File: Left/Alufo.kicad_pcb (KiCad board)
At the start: 2 copper layers, 139.7 x 88.9 mm, 67 parts, among them J1 USB_C_Receptacle_USB2.0_16P_2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, J3 USB_C_Receptacle_USB2.0_16P_2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, K11 PG1350, K12 PG1350, K13 PG1350, K14 PG1350, K15 PG1350, K16 PG1350, K21 PG1350, K22 PG1350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

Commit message: Manually add cutouts for 2010 resistors
Using middle-layer cutouts defined in the footprint no longer works as the resistors are now vertically aligned in relation to each rather than a set distance from the switch sockets.
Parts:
- R12, R13, R14, R15, R16: footprint Project Library:R_2010_5025Metric_Mod -> Resistor_SMD:R_2010_5025Metric
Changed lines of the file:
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@@
 		)
 	)
-	(footprint "Project Library:R_2010_5025Metric_Mod"
+	(footprint "Resistor_SMD:R_2010_5025Metric"
 		(layer "F.Cu")
 		(at 189.22 54.291679 -90)
@@
 		(tags "resistor")
 		(property "Reference" "R12"
-			(at 0 0 90)
+			(at 0 0 -90)
 			(layer "F.SilkS")
 			(effects
@@
 		)
 		(property "Value" "0R"
-			(at 0 2.28 90)
+			(at 0 2.28 -90)
 			(layer "F.Fab")
 			(effects
@@
 			)
 		)
-		(property "Footprint" "Project Library:R_2010_5025Metric_Mod"
+		(property "Footprint" "Resistor_SMD:R_2010_5025Metric"
 			(at 0 0 -90)
 			(unlocked yes)
@@
 			(layer "F.Fab")
 		)
-		(fp_rect
-			(start -9 -1.825)
-			(end 9 1.825)
-			(stroke
-				(width 0.1)
-				(type default)
-			)
-			(fill none)
-			(layer "User.1")
-		)
 		(fp_text user "${REFERENCE}"
-			(at 0 0 90)
+			(at 0 0 -90)
 			(layer "F.Fab")
 			(effects
@@
 		)
 	)
-	(footprint "Project Library:R_2010_5025Metric_Mod"
+	(footprint "Resistor_SMD:R_2010_5025Metric"
 		(layer "F.Cu")
 		(at 132.07 54.291679 -90)
@@
 		(tags "resistor")
 		(property "Reference" "R15"
-			(at 0 0 90)
+			(at 0 0 -90)
 			(layer "F.SilkS")
 			(effects
@@
 		)
 		(property "Value" "0R"
-			(at 0 2.28 90)
+			(at 0 2.28 -90)
 			(layer "F.Fab")
 			(effects
@@
 			)
 		)
-		(property "Footprint" "Project Library:R_2010_5025Metric_Mod"
+		(property "Footprint" "Resistor_SMD:R_2010_5025Metric"
 			(at 0 0 -90)
 			(unlocked yes)
@@
 			(layer "F.Fab")
 		)
-		(fp_rect
-			(start -9 -1.825)
-			(end 9 1.825)
-			(stroke
-				(width 0.1)
-				(type default)
-			)
-			(fill none)
-			(layer "User.1")
-		)
 		(fp_text user "${REFERENCE}"
-			(at 0 0 90)
+			(at 0 0 -90)
 			(layer "F.Fab")
 			(effects
@@
 		)
 	)
-	(footprint "Project Library:R_2010_5025Metric_Mod"
+	(footprint "Resistor_SMD:R_2010_5025Metric"
 		(layer "F.Cu")
 		(at 109.775 64.8335 -90)
@@
 			)
 		)
-		(property "Footprint" "Project Library:R_2010_5025Metric_Mod"
+		(property "Footprint" "Resistor_SMD:R_2010_5025Metric"
 			(at 0 0 -90)
 			(unlocked yes)
@@
 			(layer "F.Fab")
 		)
-		(fp_rect
-			(start -9 -1.825)
-			(end 9 1.825)
-			(stroke
-				(width 0.1)
-				(type default)
-			)
-			(fill none)
-			(layer "User.1")
-		)
 		(fp_text user "${REFERENCE}"
 			(at 0 0 -90)
@@
 		(fp_arc
 			(start 1.749484 0.919719)
-			(mid 1.712511 0.81407)
+			(mid 1.712517 0.81407)
 			(end 1.699999 0.702842)
 			(stroke
@@
 		(fp_arc
 			(start 1.699999 -0.702843)
-			(mid 1.712528 -0.814069)
+			(mid 1.712527 -0.814069)
 			(end 1.749484 -0.919721)
 			(stroke
@@
 		(fp_arc
 			(start -1.749484 -0.919721)
-			(mid -1.638071 -1.504035)
+			(mid -1.638071 -1.504036)
 			(end -1.046711 -1.568299)
 			(stroke
@@
 		)
 	)
-	(footprint "Project Library:R_2010_5025Metric_Mod"
+	(footprint "Resistor_SMD:R_2010_5025Metric"
 		(layer "F.Cu")
 		(at 170.17 54.291679 -90)
@@
 			)
 		)
-		(property "Footprint" "Project Library:R_2010_5025Metric_Mod"
+		(property "Footprint" "Resistor_SMD:R_2010_5025Metric"
 			(at 0 0 -90)
 			(unlocked yes)
@@
 			(layer "F.Fab")
 		)
-		(fp_rect
-			(start -9 -1.825)
-			(end 9 1.825)
-			(stroke
-				(width 0.1)
-				(type default)
-			)
-			(fill none)
-			(layer "User.1")
-		)
 		(fp_text user "${REFERENCE}"
 			(at 0 0 -90)
@@
 		)
 	)
-	(footprint "Project Library:R_2010_5025Metric_Mod"
+	(footprint "Resistor_SMD:R_2010_5025Metric"
 		(layer "F.Cu")
 		(at 151.12 54.291679 -90)
@@
 			)
 		)
-		(property "Footprint" "Project Library:R_2010_5025Metric_Mod"
+		(property "Footprint" "Resistor_SMD:R_2010_5025Metric"
 			(at 0 0 -90)
 			(unlocked yes)
@@
 			(layer "F.Fab")
 		)
-		(fp_rect
-			(start -9 -1.825)
-			(end 9 1.825)
-			(stroke
-				(width 0.1)
-				(type default)
-			)
-			(fill none)
-			(layer "User.1")
-		)
 		(fp_text user "${REFERENCE}"
 			(at 0 0 -90)
@@
 		(layer "Edge.Cuts")
 	)
+	(gr_rect
+		(start 130.245 47.666677)
+		(end 133.895 57.681681)
+		(stroke
+			(width 0.1)
+			(type default)
+		)
+		(fill none)
+		(layer "User.1")
+	)
+	(gr_rect
+		(start 187.395 47.666677)
+		(end 191.045 64.666681)
+		(stroke
+			(width 0.1)
+			(type default)
+		)
+		(fill none)
+		(layer "User.1")
+	)
+	(gr_rect
+		(start 149.295 43.416676)
+		(end 152.945 60.41668)
+		(stroke
+			(width 0.1)
+			(type default)
+		)
+		(fill none)
+		(layer "User.1")
+	)
 	(gr_poly
 		(pts
@@
 		)
 		(fill none)
+		(layer "User.1")
+	)
+	(gr_rect
+		(start 107.95 56.166679)
+		(end 111.6 73.166683)
+		(stroke
+			(width 0.1)
+			(type default)
+		)
+		(fill none)
+		(layer "User.1")
+	)
+	(gr_rect
+		(start 168.345 50.808998)
+		(end 171.995 60.41668)
+		(stroke
+			(width 0.1)
+			(type default)
+		)
+		(fill none)

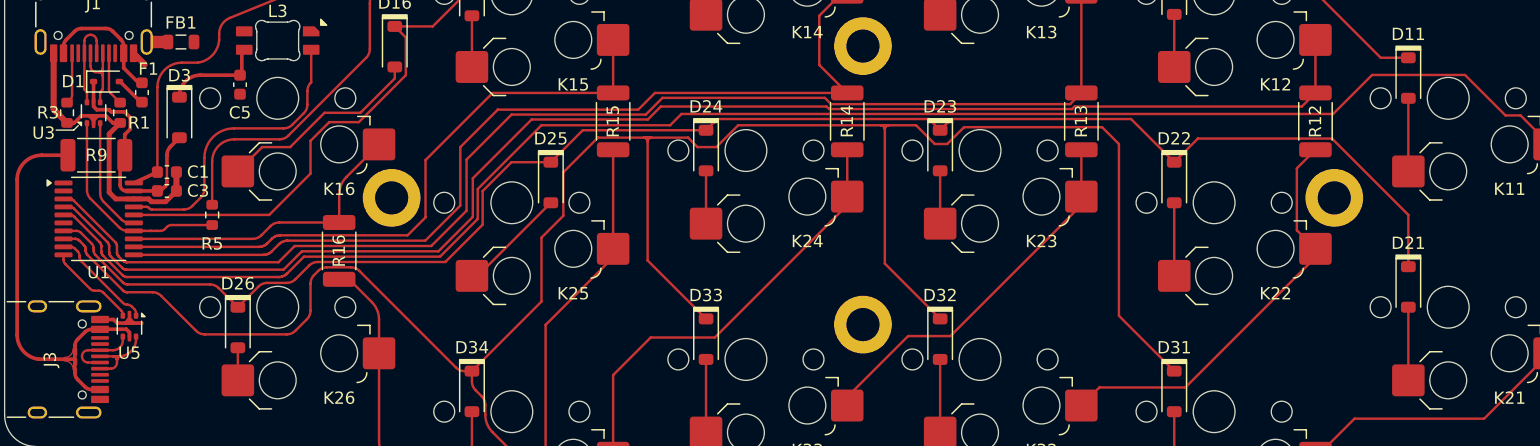
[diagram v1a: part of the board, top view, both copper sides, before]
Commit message: Clean up routing through jumper resistors
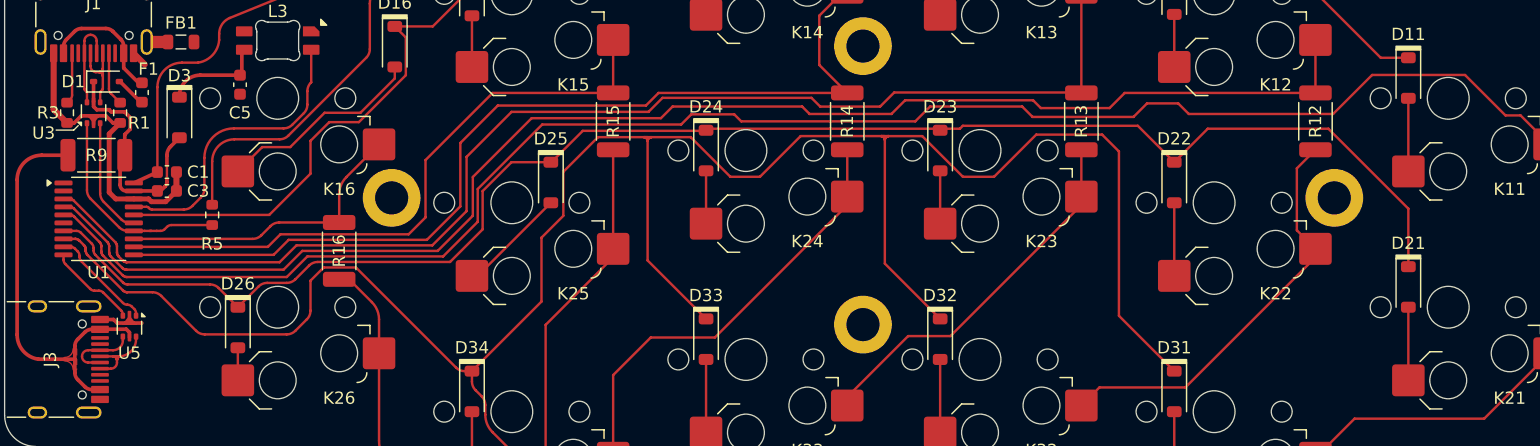
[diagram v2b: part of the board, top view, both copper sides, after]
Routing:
- net Col1: track 172.9 -> 175.0 mm
- net Col2: track 116.1 -> 117.0 mm
- net Row3: track 217.7 -> 218.6 mm

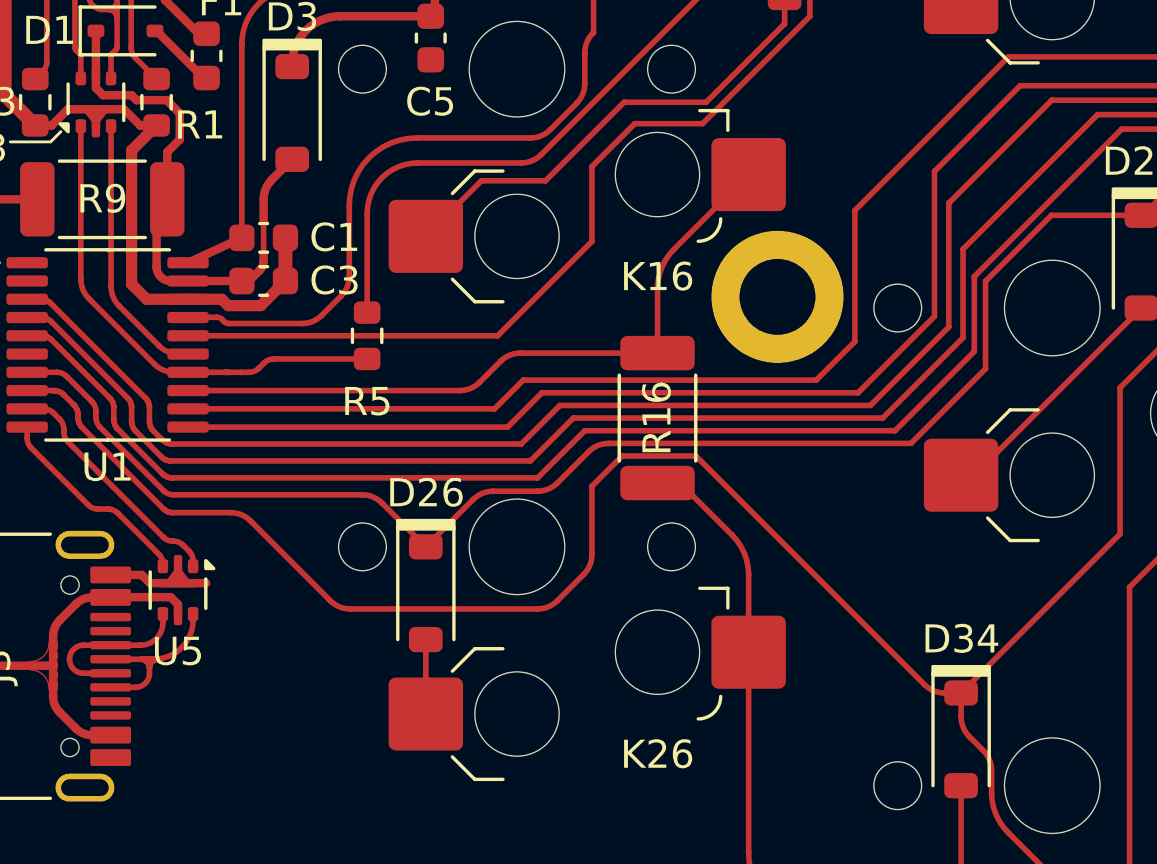
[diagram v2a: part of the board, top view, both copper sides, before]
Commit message: Align R16 with socket pads
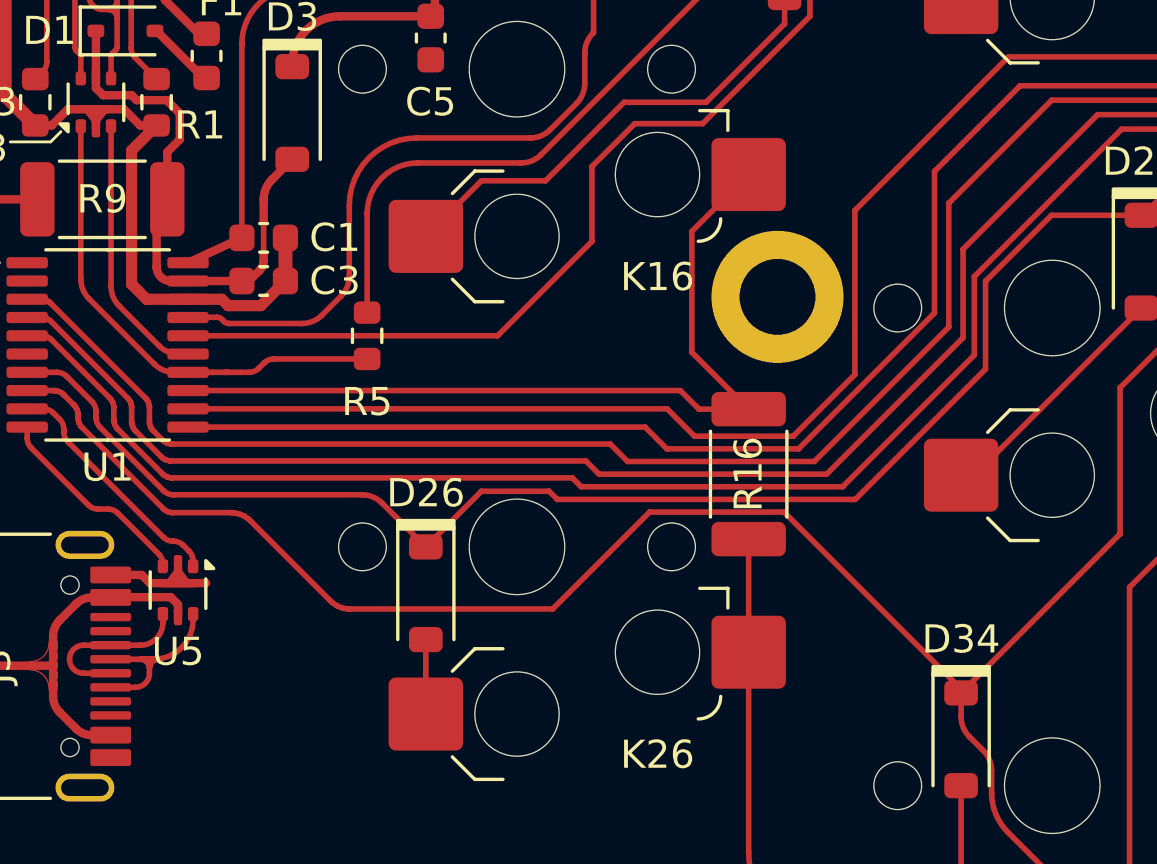
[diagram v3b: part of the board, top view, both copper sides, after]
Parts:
- moved R16 3.81 mm to (113.0, 66.8)
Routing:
- net Col6: track 24.8 -> 30.3 mm
- net Row3: track 218.6 -> 215.4 mm
- net Col6T: track 86.8 -> 83.6 mm
- net Col5: track 51.2 -> 52.7 mm
- net Col4: track 77.0 -> 77.6 mm
- net Col3: track 102.3 -> 102.8 mm

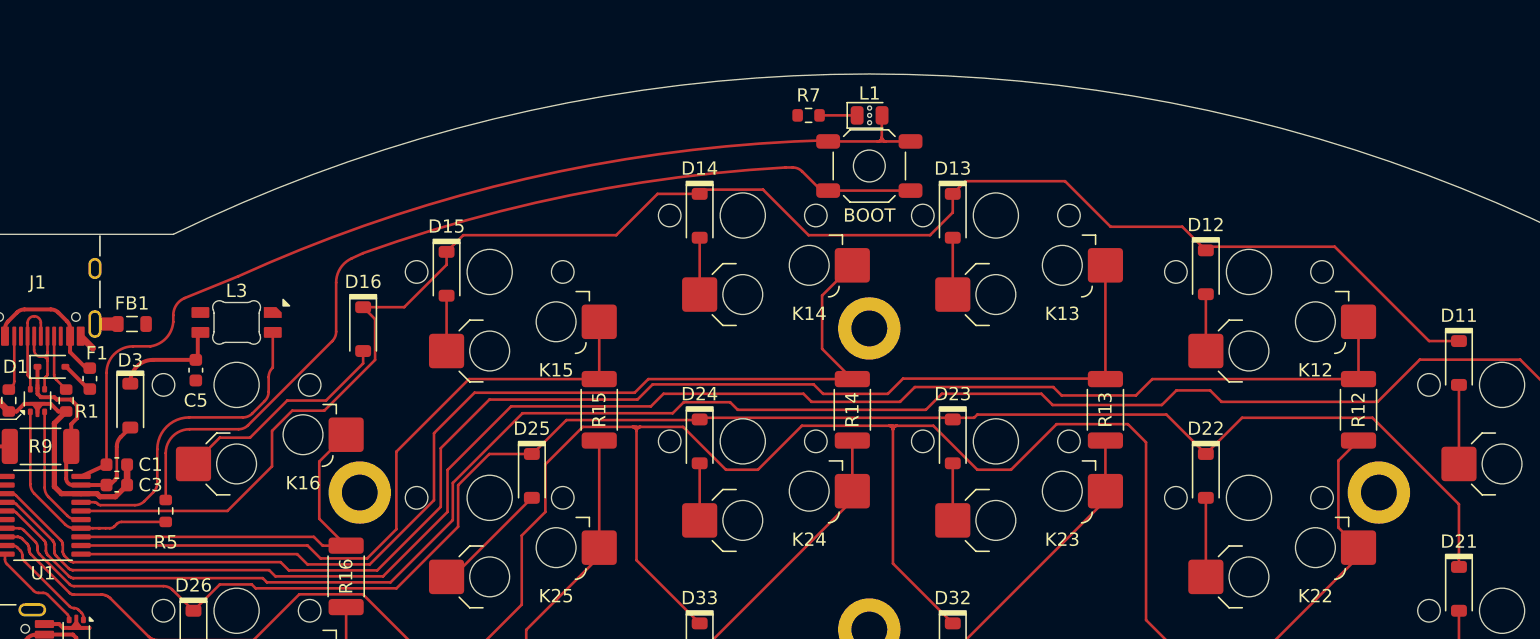
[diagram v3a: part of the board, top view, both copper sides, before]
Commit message: Move boot switch and tweak location of power LED
Boot switch is now closer to the MCU, roughly where the LED would be on the switches K15 (lefthand) or K12 (righthand). The power LED is now a little further away from the top edge.
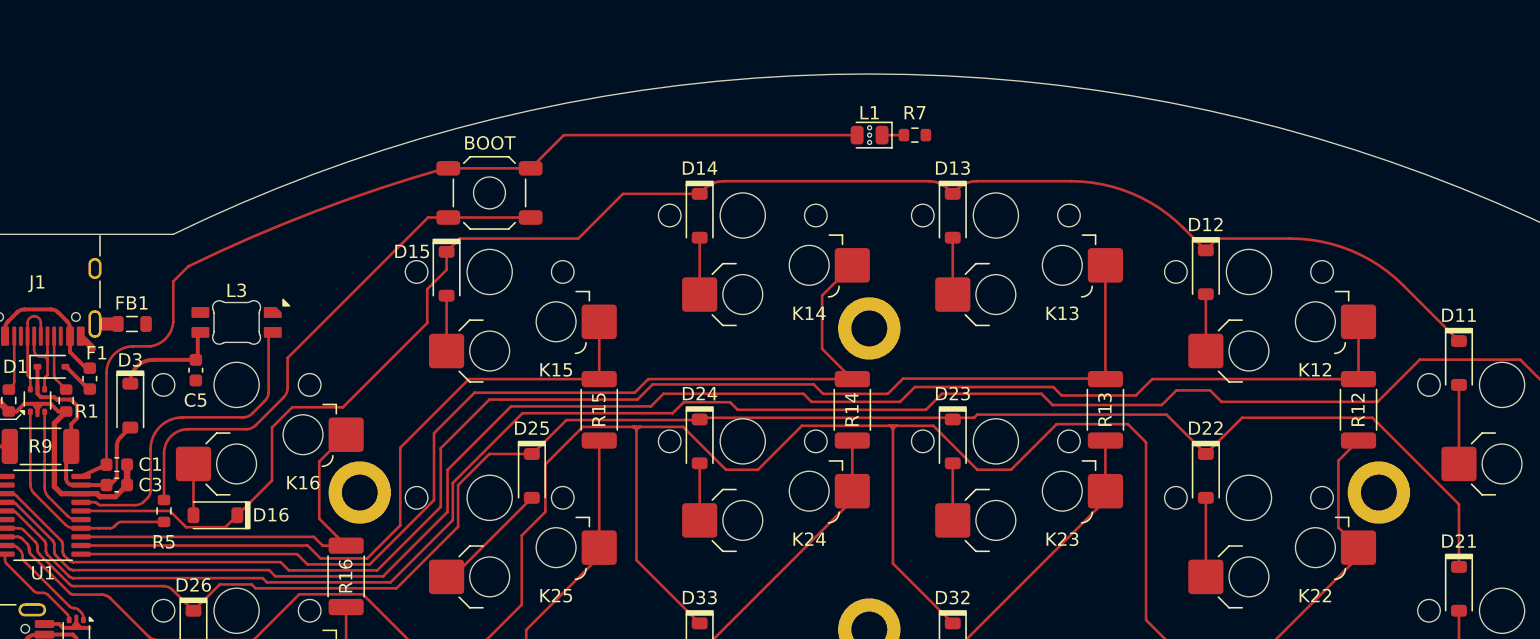
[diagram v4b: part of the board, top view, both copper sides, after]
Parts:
- moved SW1 28.7 mm to (123.8, 38.0)
- moved D16 17.9 mm to (103.2, 62.2), turned to 180 degrees
- moved R7 8.14 mm to (155.8, 33.6), turned to 0 degrees
- moved L1 1.49 mm to (152.4, 33.6), turned to 180 degrees
- moved R5 0.13 mm to (99.3, 61.9)
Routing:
- net +3V3: track 29.9 -> 52.5 mm
- net Net-(D16-A): track 16.8 -> 3.86 mm
- net BOOT: track 37.0 -> 40.1 mm
- net Row1: track 127.4 -> 124.7 mm
- net Net-(L1-K): track 2.96 -> 1.65 mm

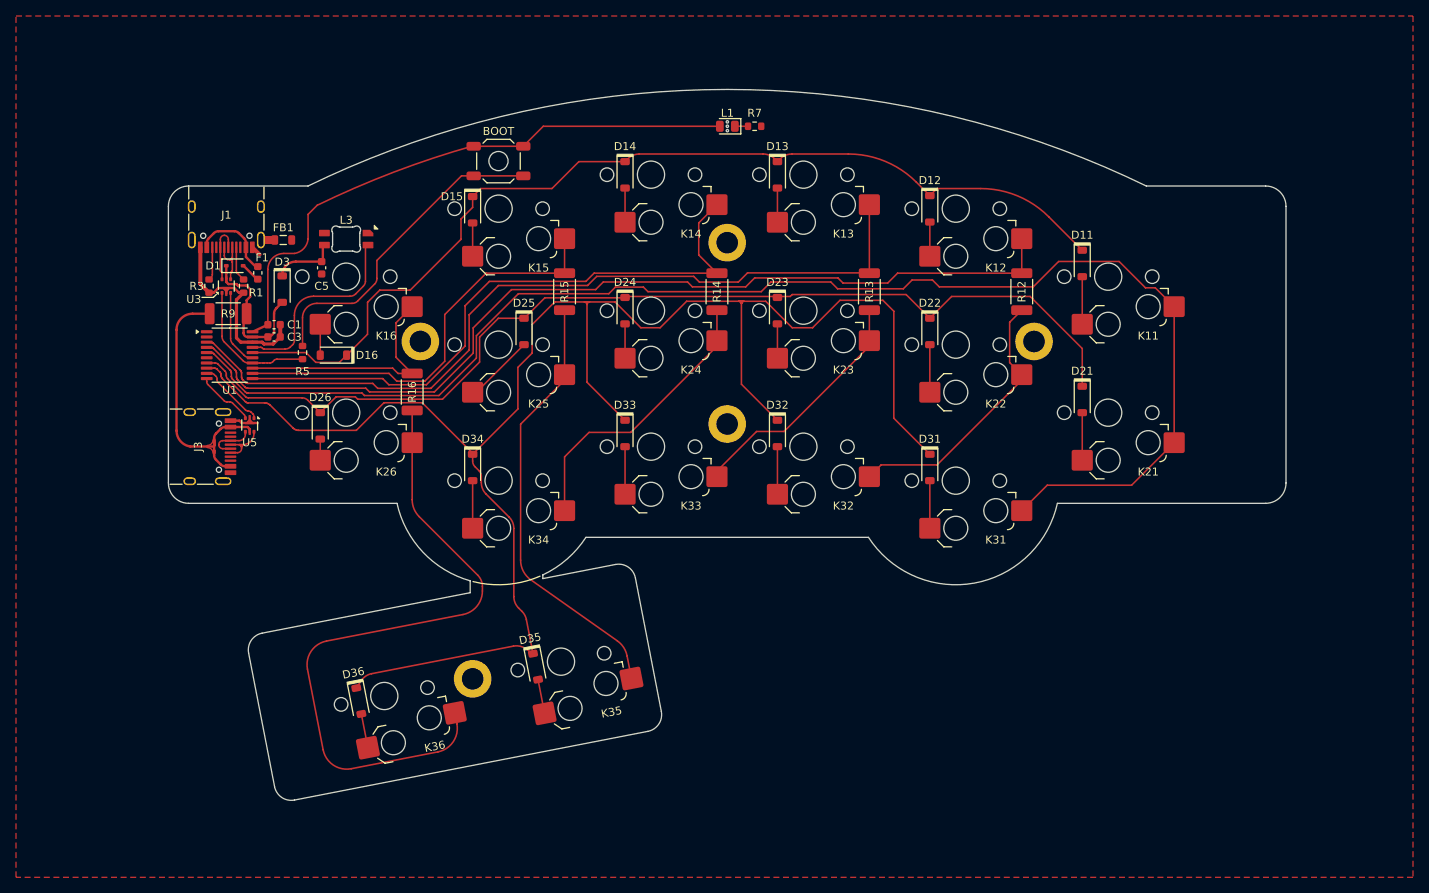
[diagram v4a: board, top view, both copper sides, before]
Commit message: Clean-up traces on lefthand board
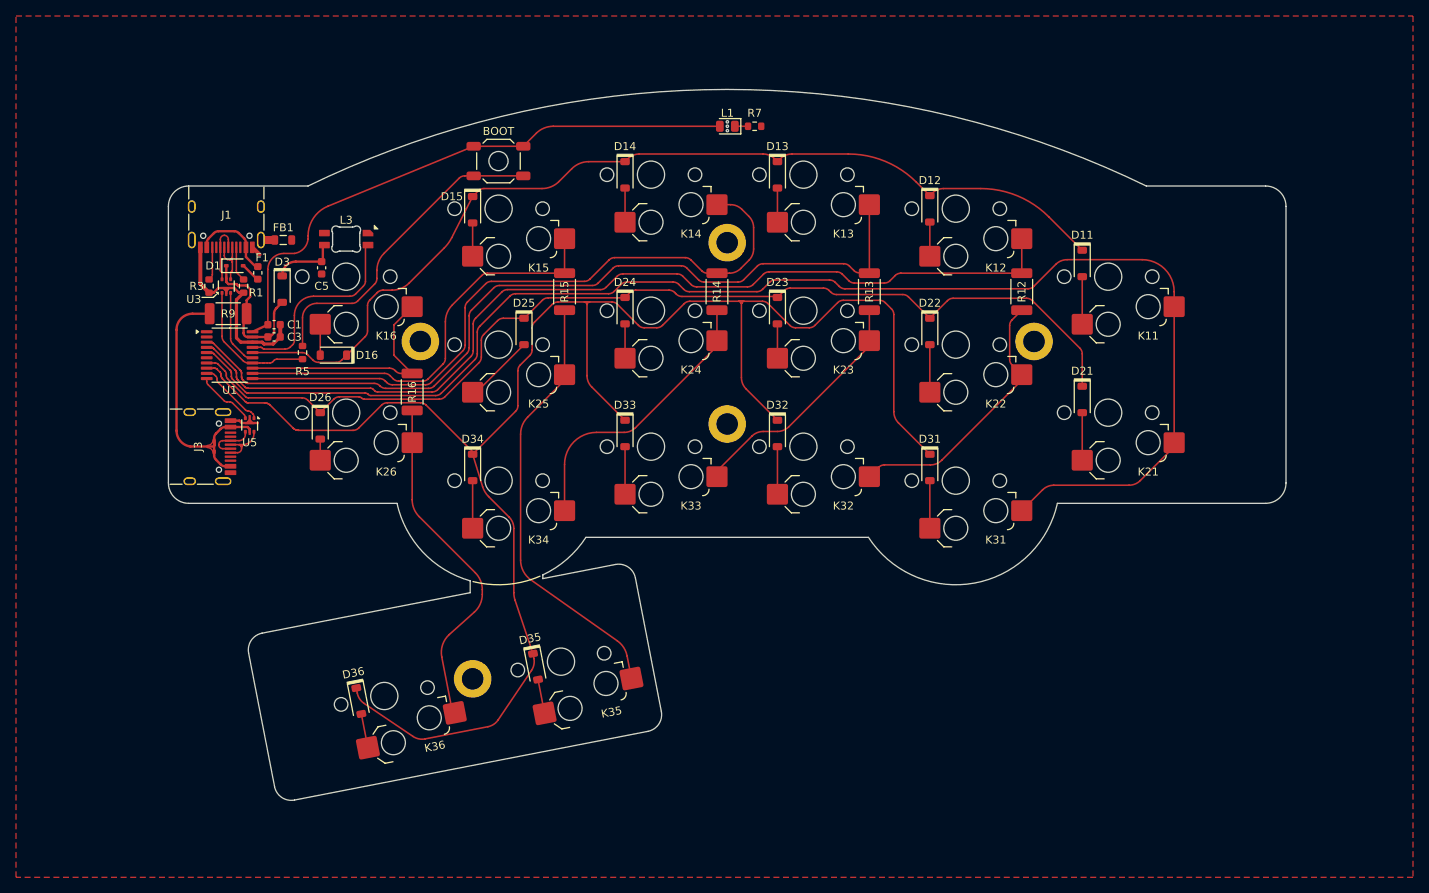
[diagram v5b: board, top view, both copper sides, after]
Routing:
- net Col6T: track 83.6 -> 43.1 mm
- net +3V3: track 52.5 -> 72.4 mm
- net Row3: track 215.4 -> 220.6 mm
- net Col4: track 77.6 -> 82.2 mm
- net Row1: track 124.7 -> 122.3 mm
- net Col2: track 117.4 -> 118.8 mm
- net Col1: track 175.3 -> 176.4 mm

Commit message: Clean-up traces on righthand board
Also make tweaks to lefthand
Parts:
- moved NT1 0.20 mm to (94.2, 63.2)
